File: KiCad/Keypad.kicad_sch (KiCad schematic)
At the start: 23 parts, among them J1 SPOX, J2 Molex, J3 USB-C, U1 ESP32-WROOM-32, U2 SP3485, U3 FT231XQ, U4 LMR16006+FB

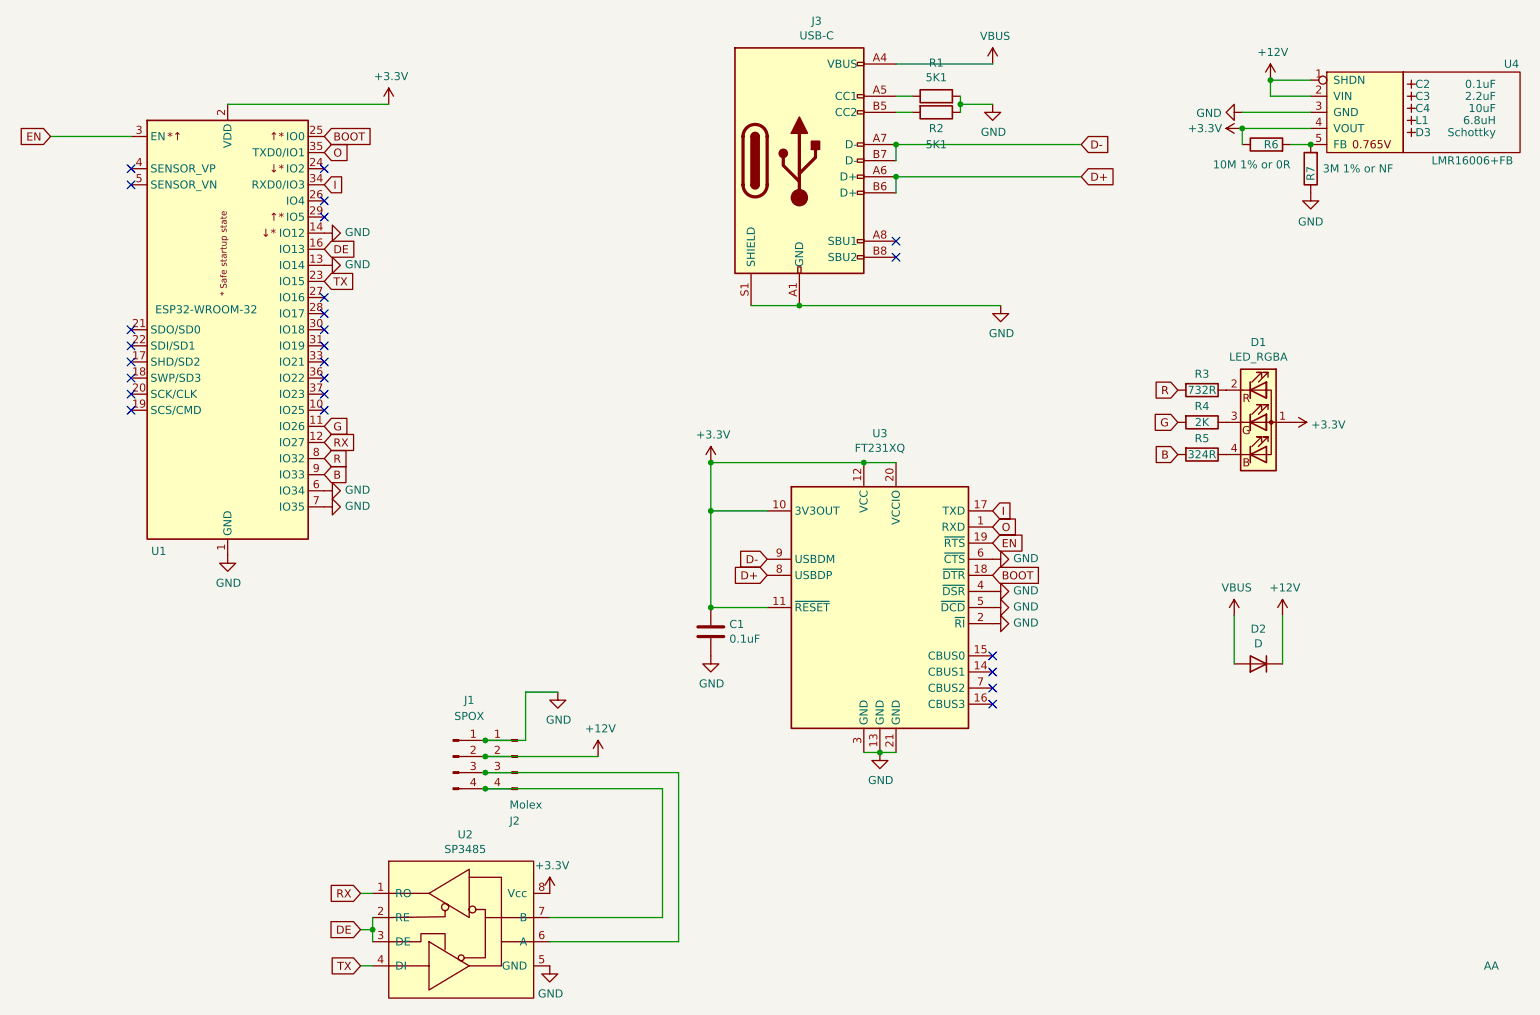
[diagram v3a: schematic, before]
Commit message: VBUS update
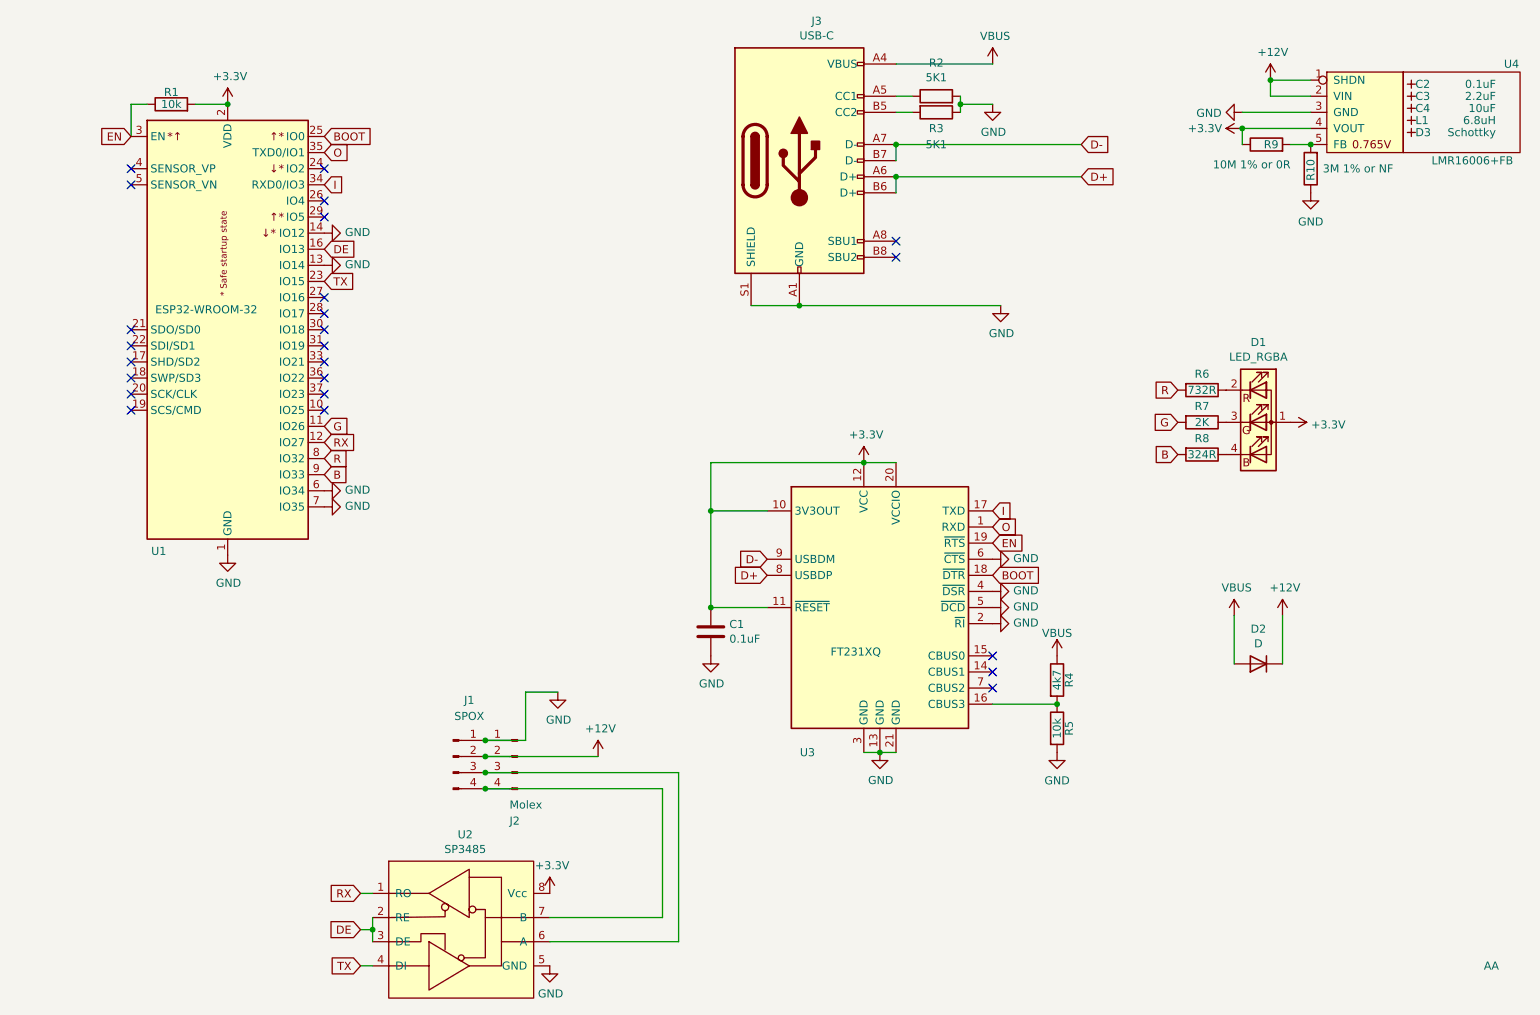
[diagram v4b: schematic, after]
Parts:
- added R1, R5: 10k, RevK:R_0603, symbol Device:R
- added R4: 4k7, RevK:R_0603, symbol Device:R
- renumbered R7 to R10, R1 to R2, R2 to R3, R3 to R6, R4 to R7, R5 to R8, R6 to R9
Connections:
- net +3V3: now also R1.2
- net EN: now also R1.1
- net GND: now also R5.2
- net VBUS: now also R4.1
- net at U3.16 (CBUS3): now also R4.2, R5.1
- no-connect marks 25 -> 24

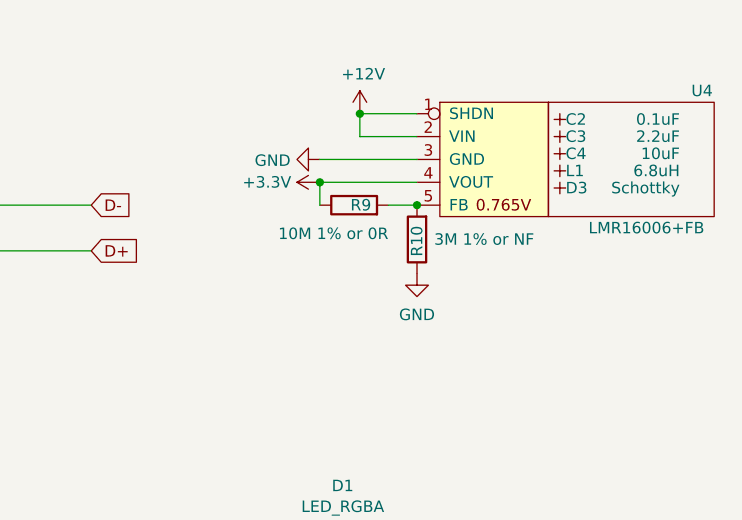
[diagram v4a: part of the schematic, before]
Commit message: Resistor fixes
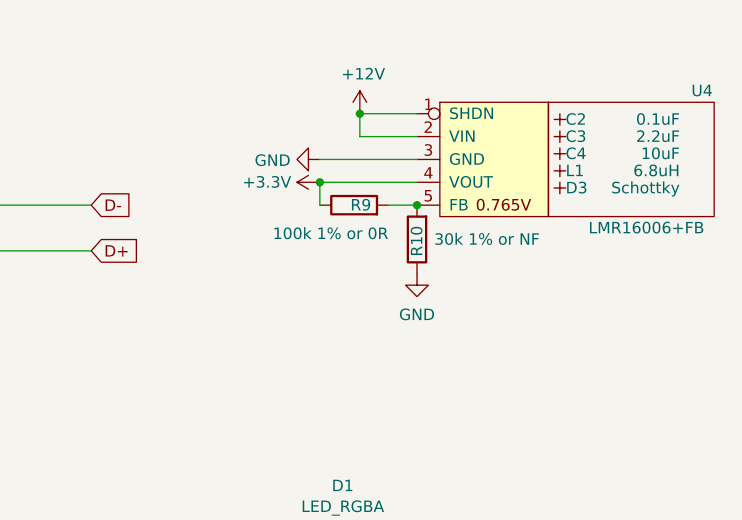
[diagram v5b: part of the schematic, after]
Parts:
- R10: value 3M 1% or NF -> 30k 1% or NF
- R9: value 10M 1% or 0R -> 100k 1% or 0R
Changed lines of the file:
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@@
       (effects (font (size 1.27 1.27)) (justify left))
     )
-    (property "Value" "10M 1% or 0R" (id 1) (at 236.855 46.355 90)
+    (property "Value" "100k 1% or 0R" (id 1) (at 236.855 46.355 90)
       (effects (font (size 1.27 1.27)) (justify left))
     )
@@
       (effects (font (size 1.27 1.27)) (justify right))
     )
-    (property "Value" "3M 1% or NF" (id 1) (at 241.935 46.99 0)
+    (property "Value" "30k 1% or NF" (id 1) (at 241.935 46.99 0)
       (effects (font (size 1.27 1.27)) (justify right))
     )
@@
     )
     (path "/0d35df78-0847-478b-9bf1-f88652133e2f"
-      (reference "R9") (unit 1) (value "10M 1% or 0R") (footprint "RevK:R_0603")
+      (reference "R9") (unit 1) (value "100k 1% or 0R") (footprint "RevK:R_0603")
     )
     (path "/fe9fc355-72ea-4cb8-a08f-1748e53389a5"
-      (reference "R10") (unit 1) (value "3M 1% or NF") (footprint "RevK:R_0603")
+      (reference "R10") (unit 1) (value "30k 1% or NF") (footprint "RevK:R_0603")
     )
     (path "/001e2ab6-998e-46c3-b909-18e1a6eca211"
